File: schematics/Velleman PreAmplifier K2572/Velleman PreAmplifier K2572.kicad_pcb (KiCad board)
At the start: 2 copper layers, 43.2 x 80 mm, 18 parts, among them J1 Conn_01x10, U1 TL072

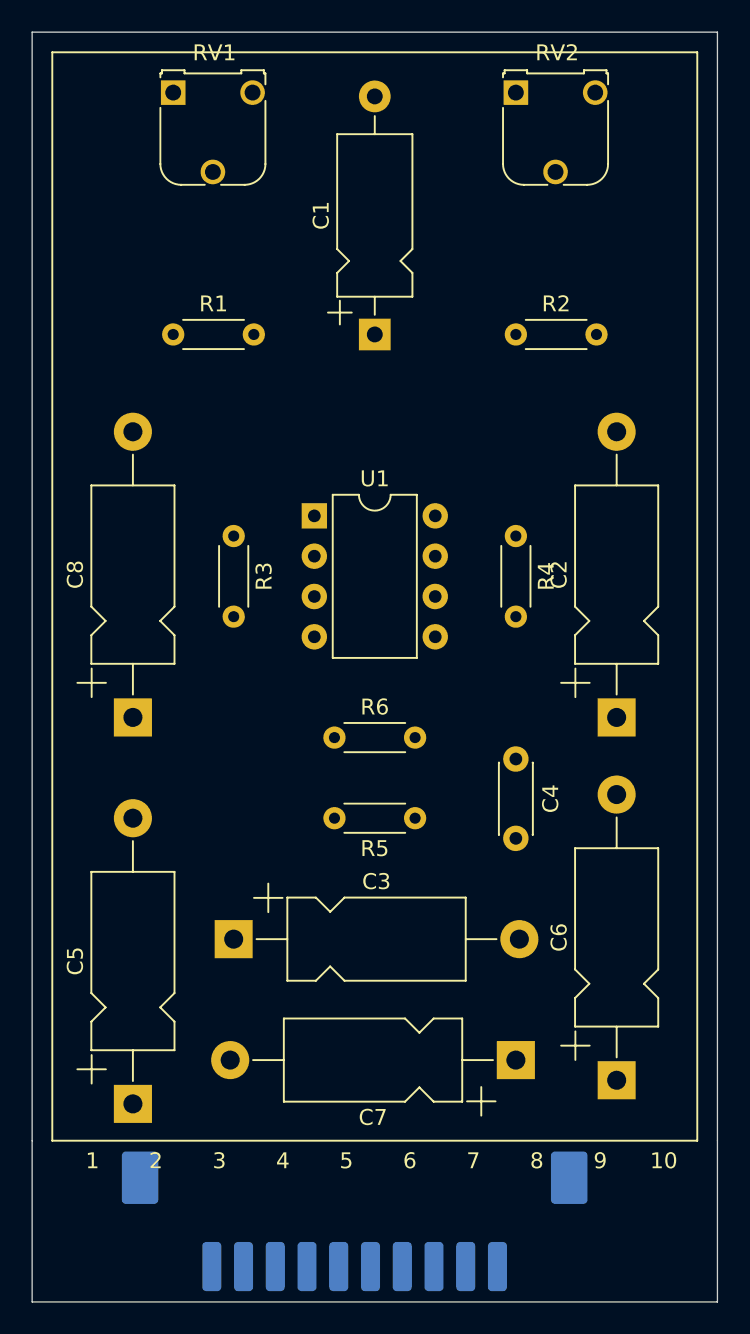
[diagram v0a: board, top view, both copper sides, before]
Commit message: Adding preamplifier 3D model
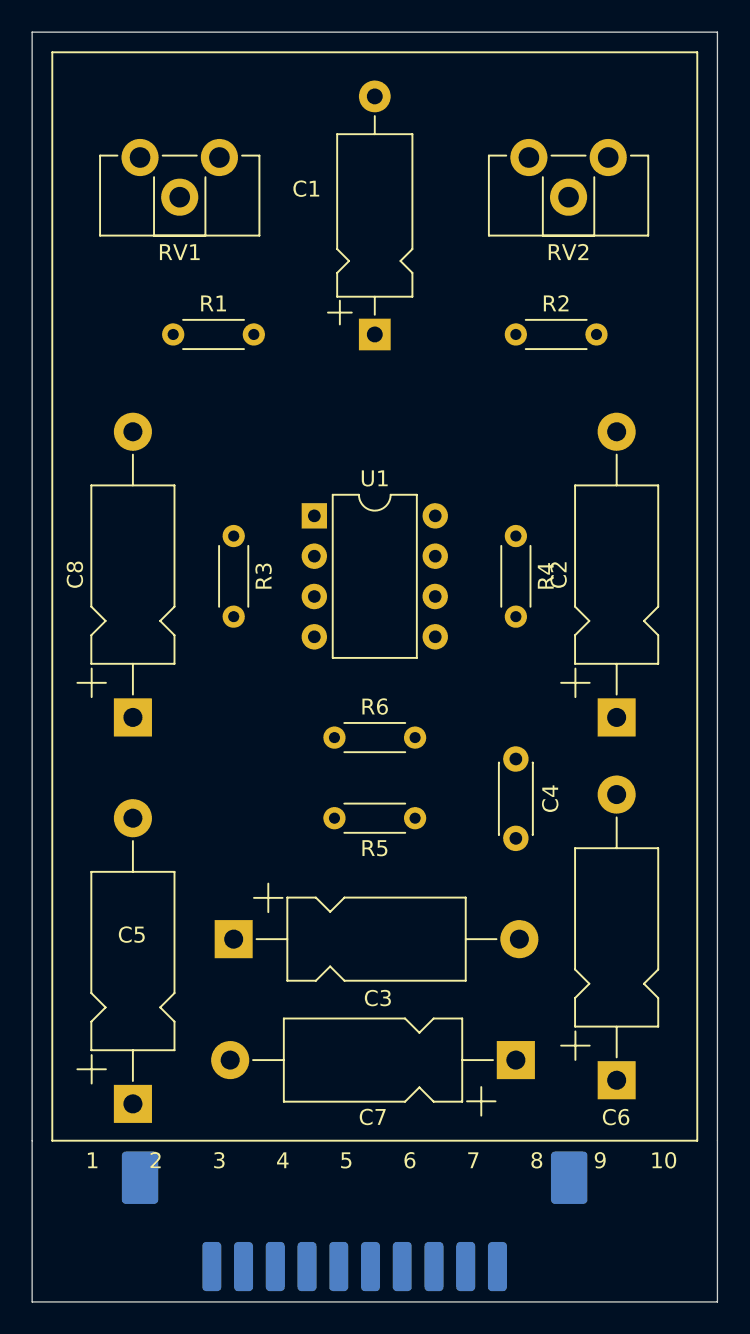
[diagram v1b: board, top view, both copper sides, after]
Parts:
- RV1, RV2: footprint Potentiometer_THT:Potentiometer_Runtron_RM-065_Vertical -> MesModules:Potentiometer_ACP_CA9-H2,5_Horizontal
- moved RV2 7.11 mm to (112.5, 109.5), turned to 270 degrees
- moved RV1 5.02 mm to (88.0, 109.5), turned to 270 degrees
